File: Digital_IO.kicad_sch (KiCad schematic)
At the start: 32 parts, among them J1 MMCX, J10 MMCX, J11 MMCX, J12 MMCX, J13 MMCX, J14 MMCX, J15 MMCX, J16 MMCX, J2 MMCX, J3 MMCX, J4 MMCX, J5 MMCX, J6 MMCX, J7 MMCX, J8 MMCX, J9 MMCX, U45 TLV75901PDRV, U46 TLV75901PDRV

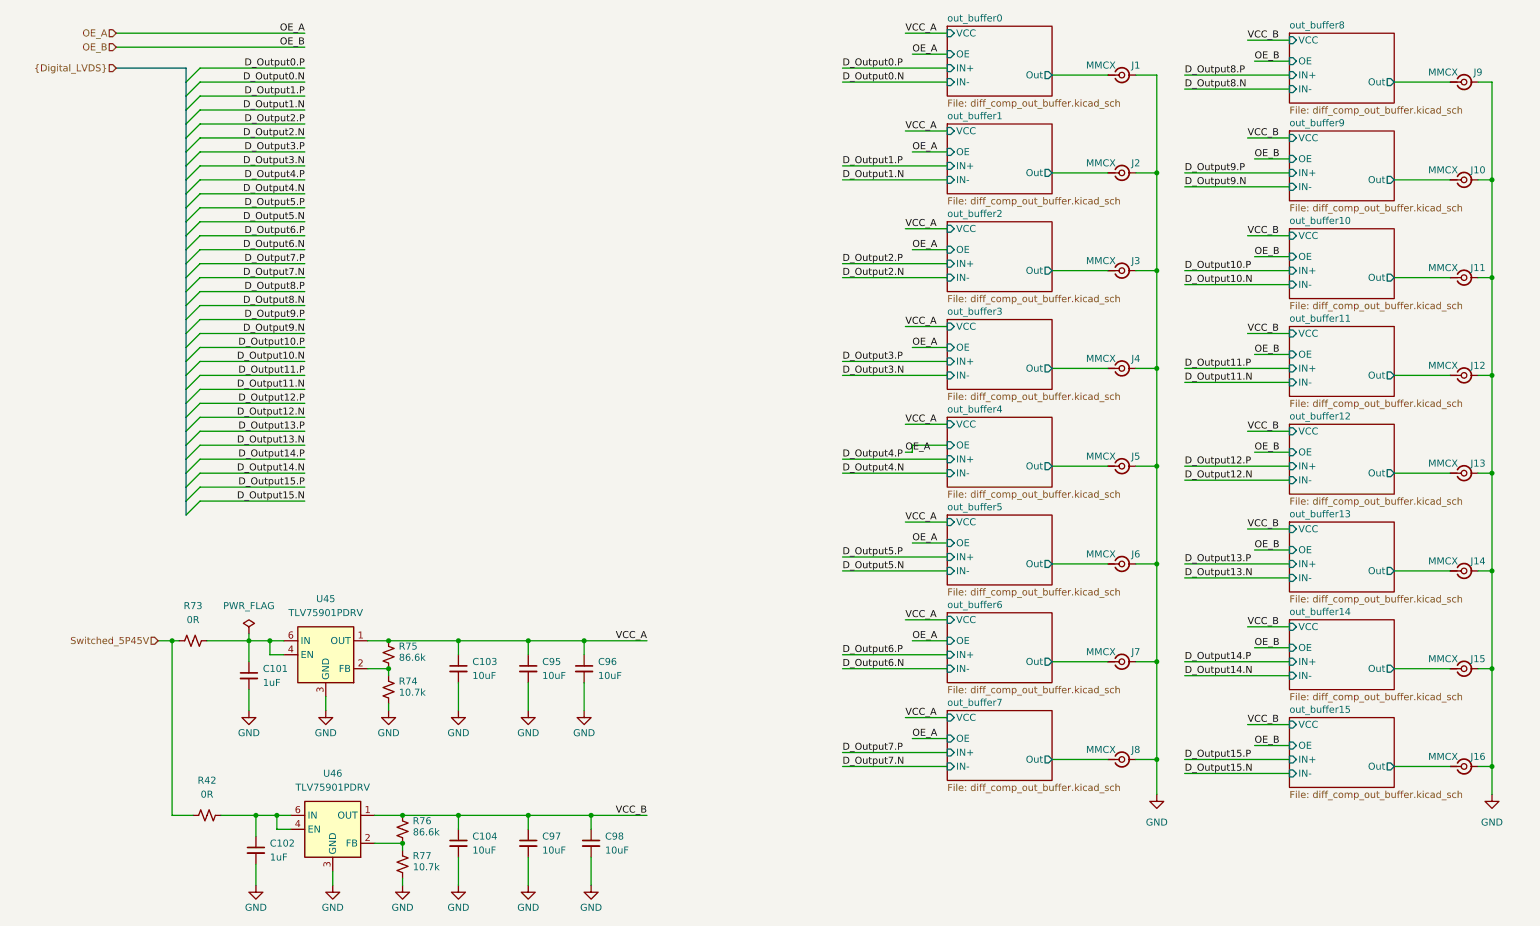
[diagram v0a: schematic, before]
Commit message: Final Draft for project
- Changed LDO for Digital Output driver to a LP3855-ADJ
- Aligned Digital Output driver sections
- Added Additional Capacitance on each digital output drive channel
- Revised Differential Lines geometry on top layer
- Revised Power routing and internal planes
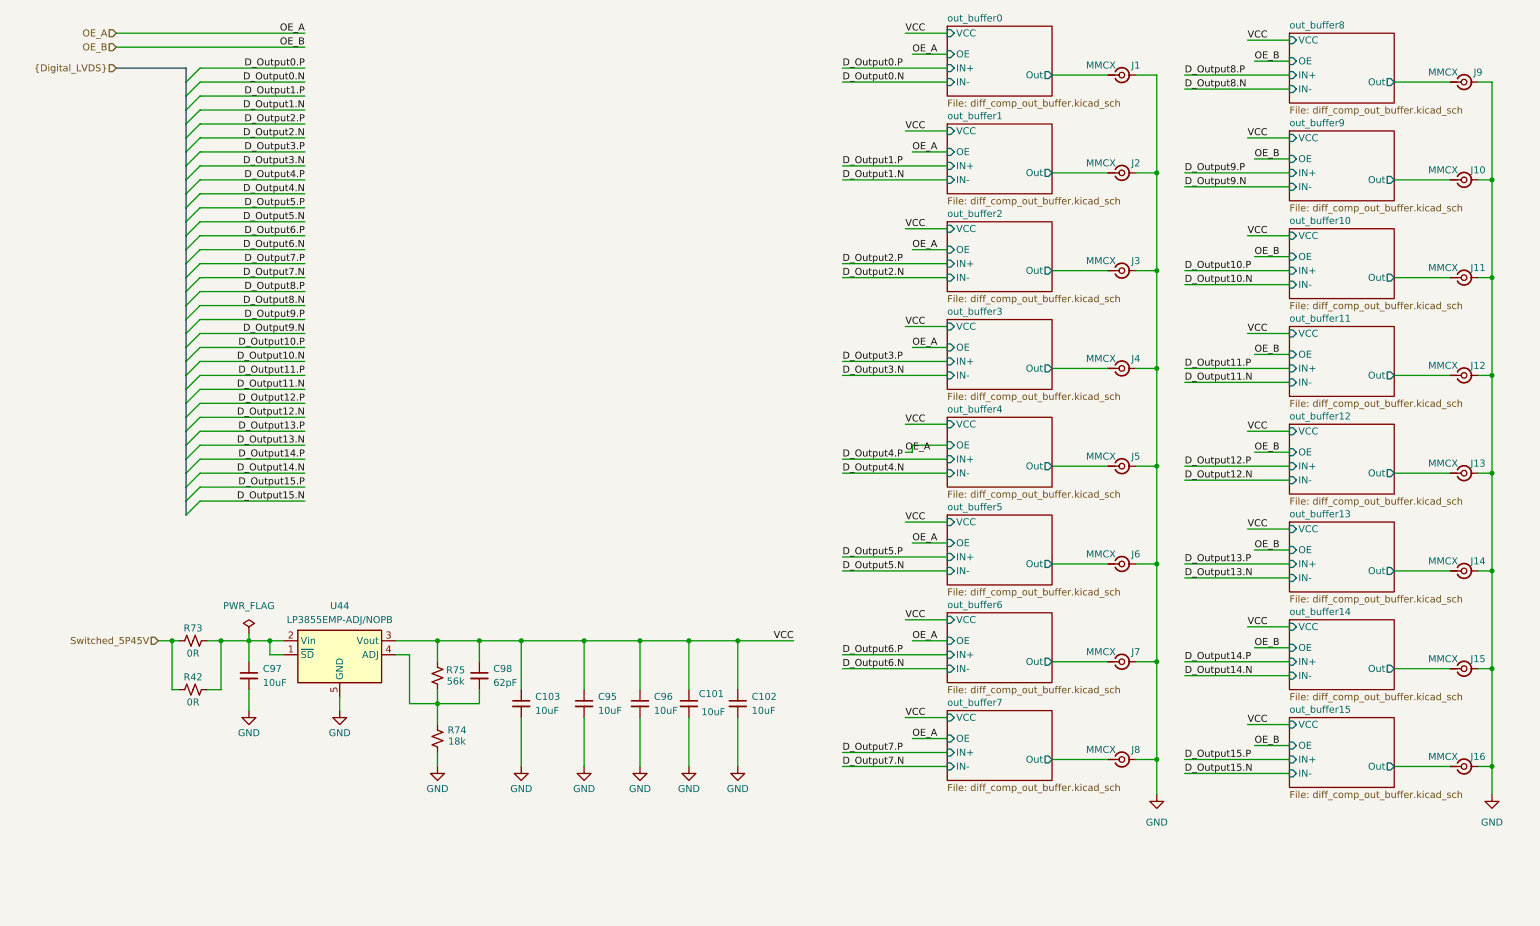
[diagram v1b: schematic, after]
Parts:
- removed C104: 10uF, Capacitor_SMD:C_0805_2012Metric, symbol Device:C_Small
- removed R76: 86.6k, Resistor_SMD:R_0402_1005Metric, symbol Device:R_Small_US
- removed R77: 10.7k, Resistor_SMD:R_0402_1005Metric, symbol Device:R_Small_US
- removed U45, U46: TLV75901PDRV, Package_SON:WSON-6-1EP_2x2mm_P0.65mm_EP1x1.6mm, symbol Regulator_Linear:TLV75801PDRV
- added U44: LP3855EMP-ADJ/NOPB, rf-input-fmc:SOT-223-5, symbol evr-fmc:LP3855-ADJ
- C101, C102: value 1uF -> 10uF; footprint Capacitor_SMD:C_0603_1608Metric -> Capacitor_SMD:C_0805_2012Metric; Digikey 490-5241-6-ND -> (none); MPN GCM188R71C105KA64D -> GRM21BR61E106KA73L
- C103, C95, C96, C97: Digikey 490-5523-6-ND -> (none)
- C98: value 10uF -> 62pF; footprint Capacitor_SMD:C_0805_2012Metric -> Capacitor_SMD:C_0603_1608Metric; Digikey 490-5523-6-ND -> (none); MPN GRM21BR61E106KA73L -> (none); Manufacturer Murata -> (none)
- J1, J10, J11, J12, J13, J14, J15, J16, J2, J3, J4, J5, J6, J7, J8, J9: Digikey SAM10617-ND -> (none)
- R42, R73: Digikey P0.0GDKR-ND -> (none)
- R74: value 10.7k -> 18k; Digikey 13-RC0402FR-1310K7LDKR-ND -> (none); MPN RC0402FR-1310K7L -> AC0402FR-0718KL
- R75: value 86.6k -> 56k; Digikey YAG3249DKR-ND -> (none); MPN RC0402FR-0786K6L -> AF0402FR-0756KL
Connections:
- net VCC_A is gone; now on net VCC: C103.1, C95.1, C96.1, R75.2
- net GND: now also U44.5 (GND); no longer C98.2
- net at R42.2: now also C97.1, R73.2, U44.1 (~{SD}), U44.2 (Vin); no longer C102.1
- net at R74.2, R75.1: now also C98.2, U44.4 (ADJ)
- net VCC: now reaches C101.1
- net VCC: now also C102.1, C98.1, U44.3 (Vout); no longer R73.2
- removed net VCC_B: C97.1, C98.1
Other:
- moved on the sheet: C103, C95, C96, R42, R74, R75

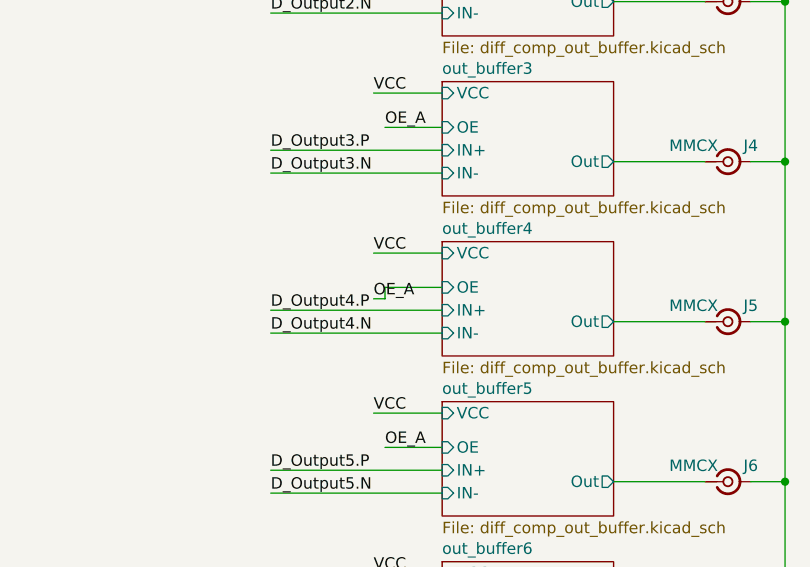
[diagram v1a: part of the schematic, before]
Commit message: Schematic and Layout Tweaks
- Updated all vias to 0.6/0.3mm
- New mechanical universal Marble holes for H2
- widen the power traces to Test points
- Add pin 4 of U20/U24 to GND net
- add a GND pour around U44 for heat
- Widen GND traces on LDOs (U24/U20)
- Grounding of unused gates of level shifters
-Small updates footprints for U18,U19,U23,U25
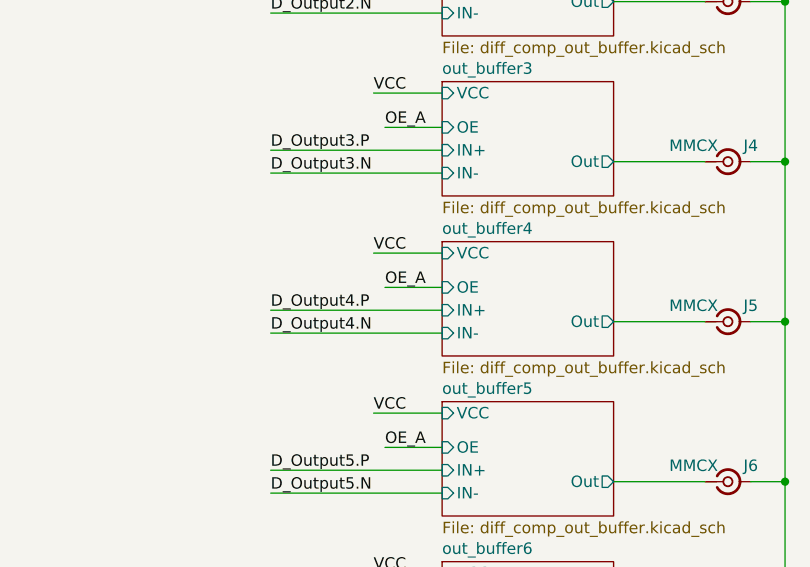
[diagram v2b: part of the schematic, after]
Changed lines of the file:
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@@
-	(wire
-		(pts
-			(xy 175.26 92.71) (xy 173.99 92.71)
-		)
-		(stroke
-			(width 0)
-			(type default)
-		)
-	)
 	(wire
 		(pts
@@
 		(pts
 			(xy 58.42 129.54) (xy 58.42 127)
-		)
-		(stroke
-			(width 0)
-			(type default)
-		)
-	)
-	(wire
-		(pts
-			(xy 175.26 92.71) (xy 175.26 91.44)
 		)
 		(stroke
@@
 	)
 	(label "OE_A"
-		(at 173.99 92.71 0)
-		(effects
-			(font
+		(at 175.26 91.44 0)
+		(effects
+			(font

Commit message: Updates after external review
- Changed Value of R66 & R67
- Added 100nF cap (C104) at input of U22
- Added GND via in center of U24 (like other LDO's)
- Changed 1nF Caps in Digital output section to 10nF
- Rounded pads of (T1-T4)
- Adjusted traces between T1-T4 and their respective MMCX connector
- Added FB1 & C136 at output of U22(5.45V switcher)
- Exchanged R88(0ohm) for a Ferrite Bead at input to U22(5.45V switcher)
- Revised layout of U22 area to more closely follow the data sheet.
- Exchanged R73&R42 at input to U44 for a ferrite bead (FB3)
- Exchanged R86/87/98/99 at input of TLV757 LDO for ferrite beads
- Added 1uF caps to VDD, VDDA, and VDDS power rails on Jitter Cleaner
- Changed C46,C47,C75,C77 from 1uF to 10uF caps
- Added Ferrite and 2 caps for each VDDO power rail on the jitter cleaners
- Adjusted layout around pint 26,27,28, of U18
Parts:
- removed R42, R73: 0R, Resistor_SMD:R_0603_1608Metric, symbol Device:R_Small_US
- added FB3: 300@100MHz, Inductor_SMD:L_0805_2012Metric, symbol Device:FerriteBead_Small
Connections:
- net Switched_5P45V: now also FB3.1
- net at C97.1, U44.1 (~{SD}), U44.2 (Vin): now also FB3.2
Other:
- note added: "50mOhm 3A"
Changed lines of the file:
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@@
 		(comment 1 "SPDX-License-Identifier: CERN-OHL-S-2.0+")
 	)
+	(text "50mOhm\n3A"
+		(exclude_from_sim no)
+		(at 44.45 133.35 0)
+		(effects
+			(font
+				(size 1.27 1.27)
+			)
+		)
+	)
 	(junction
 		(at 280.67 114.3)
@@
 	)
 	(junction
-		(at 40.64 127)
-		(diameter 0)
-		(color 0 0 0 0)
-	)
-	(junction
 		(at 219.71 59.69)
 		(diameter 0)
@@
 	)
 	(junction
-		(at 49.53 127)
-		(diameter 0)
-		(color 0 0 0 0)
-	)
-	(junction
 		(at 280.67 78.74)
 		(diameter 0)
@@
 	(wire
 		(pts
-			(xy 40.64 135.89) (xy 40.64 127)
-		)
-		(stroke
-			(width 0)
-			(type default)
-		)
-	)
-	(wire
-		(pts
 			(xy 64.77 27.94) (xy 45.72 27.94)
 		)
@@
 	(wire
 		(pts
-			(xy 49.53 135.89) (xy 49.53 127)
-		)
-		(stroke
-			(width 0)
-			(type default)
-		)
-	)
-	(wire
-		(pts
 			(xy 54.61 135.89) (xy 54.61 139.7)
 		)
@@
 		)
 	)
-	(wire
-		(pts
-			(xy 46.99 135.89) (xy 49.53 135.89)
-		)
-		(stroke
-			(width 0)
-			(type default)
-		)
-	)
 	(bus
 		(pts
@@
 	(wire
 		(pts
-			(xy 49.53 127) (xy 54.61 127)
-		)
-		(stroke
-			(width 0)
-			(type default)
-		)
-	)
-	(wire
-		(pts
 			(xy 224.79 44.45) (xy 243.84 44.45)
 		)
@@
 	(wire
 		(pts
-			(xy 40.64 127) (xy 41.91 127)
+			(xy 38.1 127) (xy 41.91 127)
 		)
 		(stroke
@@
 	(wire
 		(pts
-			(xy 38.1 127) (xy 40.64 127)
-		)
-		(stroke
-			(width 0)
-			(type default)
-		)
-	)
-	(wire
-		(pts
 			(xy 273.05 25.4) (xy 262.89 25.4)
 		)
@@
 	(wire
 		(pts
-			(xy 41.91 135.89) (xy 40.64 135.89)
-		)
-		(stroke
-			(width 0)
-			(type default)
-		)
-	)
-	(wire
-		(pts
 			(xy 181.61 55.88) (xy 175.26 55.88)
 		)
@@
 	(wire
 		(pts
-			(xy 46.99 127) (xy 49.53 127)
+			(xy 46.99 127) (xy 54.61 127)
 		)
 		(stroke
@@
 	)
 	(symbol
-		(lib_id "Device:R_Small_US")
-		(at 44.45 135.89 90)
-		(unit 1)
-		(exclude_from_sim no)
-		(in_bom yes)
-		(on_board yes)
-		(dnp no)
-		(property "Reference" "R42"
-			(at 44.45 133.604 90)
-			(effects
-				(font
-					(size 1.27 1.27)
-				)
-			)
-		)
-		(property "Value" "0R"
-			(at 44.45 138.176 90)
-			(effects
-				(font
-					(size 1.27 1.27)
-				)
-			)
-		)
-		(property "Footprint" "Resistor_SMD:R_0603_1608Metric"
-			(at 44.45 135.89 0)
-			(effects
-				(font
-					(size 1.27 1.27)
-				)
-				(hide yes)
-			)
-		)
-		(property "Datasheet" "~"
-			(at 44.45 135.89 0)
-			(effects
-				(font
-					(size 1.27 1.27)
-				)
-				(hide yes)
-			)
-		)
-		(property "Description" "RES SMD 0 OHM JUMPER 1/10W 0603"
-			(at 44.45 135.89 0)
-			(effects
-				(font
-					(size 1.27 1.27)
-				)
-				(hide yes)
-			)
-		)
-		(property "MPN" "ERJ-3GEY0R00V"
-			(at 44.45 135.89 90)
-			(effects
-				(font
-					(size 1.27 1.27)
-				)
-				(hide yes)
-			)
-		)
-		(property "Manufacturer" "Panasonic Electronic Components"
-			(at 44.45 135.89 90)
-			(effects
-				(font
-					(size 1.27 1.27)
-				)
-				(hide yes)
-			)
-		)
-		(pin "1"
-		)
-		(pin "2"
-		)
-		(instances
-			(project "evr-fmc"
-				(path "/1719e569-47c8-4fa0-8523-9c9686ef0dba/e8674f3d-4c31-47ac-9c13-b31bc6bb3cc0"
-					(reference "R42")
-					(unit 1)
-				)
-			)
-		)
-	)
-	(symbol
 		(lib_id "Connector:Conn_Coaxial_Small")
 		(at 213.36 148.59 0)
@@
 	)
 	(symbol
-		(lib_id "Device:C_Small")
-		(at 96.52 133.35 0)
+		(lib_id "Device:FerriteBead_Small")
+		(at 44.45 127 90)
 		(unit 1)
 		(exclude_from_sim no)
@@
 		(on_board yes)
 		(dnp no)
-		(fields_autoplaced yes)
-		(property "Reference" "C98"
-			(at 99.06 132.0862 0)
+		(property "Reference" "FB3"
+			(at 44.45 123.952 90)
 			(effects
 				(font
 					(size 1.27 1.27)
 				)
-				(justify left)
 			)
 		)
-		(property "Value" "62pF"
-			(at 99.06 134.6262 0)
+		(property "Value" "300@100MHz"
+			(at 44.45 130.048 90)
 			(effects
 				(font
 					(size 1.27 1.27)
 				)
-				(justify left)
 			)
 		)
-		(property "Footprint" "Capacitor_SMD:C_0603_1608Metric"
-			(at 96.52 133.35 0)
+		(property "Footprint" "Inductor_SMD:L_0805_2012Metric"
+			(at 44.45 128.778 90)
 			(effects
 				(font
@@
 		)
 		(property "Datasheet" "~"
-			(at 96.52 133.35 0)
+			(at 44.45 127 0)
 			(effects
 				(font
@@
 			)
 		)
-		(property "Description" ""
-			(at 96.52 133.35 0)
+		(property "Description" "FERRITE BEAD 300 OHM 0805 3LN"
+			(at 44.45 127 0)
 			(effects
 				(font
@@
 			)
 		)
-		(property "MPN" ""
-			(at 96.52 133.35 0)
+		(property "MPN" "742792031"
+			(at 44.45 127 90)
 			(effects
 				(font
@@
 			)
 		)
-		(property "Manufacturer" ""
-			(at 96.52 133.35 0)
+		(property "Manufacturer" "Würth Elektronik"
+			(at 44.45 127 90)
 			(effects
 				(font
@@
 			(project "trigger-output-fmc"
 				(path "/1719e569-47c8-4fa0-8523-9c9686ef0dba/e8674f3d-4c31-47ac-9c13-b31bc6bb3cc0"
-					(reference "C98")
+					(reference "FB3")
 					(unit 1)
 				)
@@
 	)
 	(symbol
-		(lib_id "Connector:Conn_Coaxial_Small")
-		(at 275.59 43.18 0)
-		(mirror x)
+		(lib_id "Device:C_Small")
+		(at 96.52 133.35 0)
 		(unit 1)
 		(exclude_from_sim no)
@@
 		(on_board yes)
 		(dnp no)
-		(property "Reference" "J10"
-			(at 278.13 41.402 0)
+		(fields_autoplaced yes)
+		(property "Reference" "C98"
+			(at 99.06 132.0862 0)
 			(effects
 				(font
 					(size 1.27 1.27)
 				)
+				(justify left)
 			)
 		)
-		(property "Value" "MMCX"
-			(at 271.78 41.402 0)
+		(property "Value" "62pF"
+			(at 99.06 134.6262 0)
 			(effects
 				(font
 					(size 1.27 1.27)
 				)
+				(justify left)
 			)
 		)
-		(property "Footprint" "Connector_Coaxial:MMCX_Molex_73415-1471_Vertical"
-			(at 275.59 43.18 0)
+		(property "Footprint" "Capacitor_SMD:C_0603_1608Metric"
+			(at 96.52 133.35 0)
 			(effects
 				(font
@@
 		)
 		(property "Datasheet" "~"
-			(at 275.59 43.18 0)
+			(at 96.52 133.35 0)
 			(effects
 				(font
@@
 			)
 		)
-		(property "Description" "CONN MMCX JACK STR 50 OHM PCB"
-			(at 275.59 43.18 0)
+		(property "Description" ""
+			(at 96.52 133.35 0)
 			(effects
 				(font
@@
 			)
 		)
-		(property "MPN" "MMCX-J-P-H-ST-TH1"
-			(at 275.59 43.18 0)
+		(property "MPN" ""
+			(at 96.52 133.35 0)
 			(effects
 				(font
@@
 			)
 		)
-		(property "Manufacturer" "Samtec Inc."
-			(at 275.59 43.18 0)
+		(property "Manufacturer" ""
+			(at 96.52 133.35 0)
 			(effects
 				(font
@@
 			)
 		)
-		(pin "1"
-		)
 		(pin "2"
 		)
+		(pin "1"
+		)
 		(instances
-			(project "evr-fmc"
+			(project "trigger-output-fmc"
 				(path "/1719e569-47c8-4fa0-8523-9c9686ef0dba/e8674f3d-4c31-47ac-9c13-b31bc6bb3cc0"
-					(reference "J10")
+					(reference "C98")
 					(unit 1)
 				)
@@
 	)
 	(symbol
-		(lib_id "Device:R_Small_US")
-		(at 44.45 127 90)
+		(lib_id "Connector:Conn_Coaxial_Small")
+		(at 275.59 43.18 0)
+		(mirror x)
 		(unit 1)
 		(exclude_from_sim no)
@@
 		(on_board yes)
 		(dnp no)
-		(property "Reference" "R73"
-			(at 44.45 124.714 90)
+		(property "Reference" "J10"
+			(at 278.13 41.402 0)
 			(effects
 				(font
@@
 			)
 		)
-		(property "Value" "0R"
-			(at 44.45 129.286 90)
+		(property "Value" "MMCX"
+			(at 271.78 41.402 0)
 			(effects
 				(font
@@
 			)
 		)
-		(property "Footprint" "Resistor_SMD:R_0603_1608Metric"
-			(at 44.45 127 0)
+		(property "Footprint" "Connector_Coaxial:MMCX_Molex_73415-1471_Vertical"
+			(at 275.59 43.18 0)
 			(effects
 				(font
@@
 		)
 		(property "Datasheet" "~"
-			(at 44.45 127 0)
+			(at 275.59 43.18 0)
 			(effects
 				(font
@@
 			)
 		)
-		(property "Description" "RES SMD 0 OHM JUMPER 1/10W 0603"
-			(at 44.45 127 0)
+		(property "Description" "CONN MMCX JACK STR 50 OHM PCB"
+			(at 275.59 43.18 0)
 			(effects
 				(font
@@
 			)
 		)
-		(property "MPN" "ERJ-3GEY0R00V"
-			(at 44.45 127 90)
+		(property "MPN" "MMCX-J-P-H-ST-TH1"
+			(at 275.59 43.18 0)
 			(effects
 				(font
@@
 			)
 		)
-		(property "Manufacturer" "Panasonic Electronic Components"
-			(at 44.45 127 90)
+		(property "Manufacturer" "Samtec Inc."
+			(at 275.59 43.18 0)
 			(effects
 				(font
@@
 			(project "evr-fmc"
 				(path "/1719e569-47c8-4fa0-8523-9c9686ef0dba/e8674f3d-4c31-47ac-9c13-b31bc6bb3cc0"
-					(reference "R73")
+					(reference "J10")
 					(unit 1)
 				)

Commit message: Updates after external review
- Removed various construction lines on comments layer
- Corrected various 50ohm SE traces on external layers to 0.26mm width
- Shortened up longer traces where possible on external layers and LVDS (in5)
- Made routing of CLK signals to MMCX test ports consistant

- MAJOR UPDATE to XTAL (Y1&Y2)
This now follows the family reference manual to properly isolate the XTAL
This then required the following changes:
- Swapped layer In2 with In5 (to keep LVDS between GND layers)
- Swapped layer In3 with In4 (to keep LVDS between GND layers)
- Revised gate mapping of level shifted signals on the IC (no FMC pinout change)
- Significant revision to  routing around these area
- Rounded XTAL pads
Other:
- note added: "5V Out Vout= 1.216(1+(R1/R2))"
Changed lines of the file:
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@@
 		(comment 1 "SPDX-License-Identifier: CERN-OHL-S-2.0+")
+	)
+	(text "5V Out\nVout= 1.216(1+(R1/R2))"
+		(exclude_from_sim no)
+		(at 71.12 146.812 0)
+		(effects
+			(font
+				(size 1.27 1.27)
+			)
+		)
 	)
 	(text "50mOhm\n3A"

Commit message: Small Tweaks
- Updated readme with kicad version
- fixed break in ground plane near Y2
- added exclusions with written exceptions for 4 DRC errors (where we grounded level shifter gates)
- Fixed whitespace at the end of MPNs
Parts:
- U44: MPN LP3855EMP-ADJ/NOPB -> LP3855EMP-ADJ/NOPB
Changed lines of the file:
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@@
 			)
 		)
-		(property "MPN" "LP3855EMP-ADJ/NOPB "
+		(property "MPN" "LP3855EMP-ADJ/NOPB"
 			(at 71.12 129.54 0)
 			(effects
